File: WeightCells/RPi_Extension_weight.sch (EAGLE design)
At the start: 23 parts, among them U1 AD7730BRUZ, U2 AD7730BRUZ, U3 AD7730BRUZ, U4 AD7730BRUZ, U5 AD7730BRUZ, U6 AD7730BRUZ, U7 AD7730BRUZ, U8 AD7730BRUZ, U9 STM32F103RCT6

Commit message: updated scale board
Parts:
- removed U3, U4, U5, U6, U7, U8: AD7730BRUZ, AD7730BRUZ:AD7730BRUZ
- added C2, C3, C4, C5, C6: (no value), rcl:C-EUC0603
- added SV4: (no value), con-lstb:MA03-2
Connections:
- new net N$2: SV1.1
- new net N$3: SV1.4
- new net N$4: SV1.3
- new net NRST: SV4.6, U9.NRST
- new net SPI1_MISO: U1.DOUT, U2.DOUT, U9.PA6
- new net SPI1_MOSI: U1.DIN, U2.DIN, U9.PA7
- new net SPI1_SCK: U1.SCLK, U2.SCLK, U9.PA5
- new net SS1: U1.*CS, U9.PC6
- new net SS2: U2.*CS, U9.PC7
- new net SS3: U9.PC8
- new net SS4: U9.PC9
- new net SS5: U9.PA8
- new net SS6: U9.PA9
- new net SS7: U9.PA10
- new net SS8: U9.PA11
- new net SS_STACK: SJ5.2, SJ6.2, SJ7.2, SJ8.2
- new net SWDCLK: SV4.3, U9.PA14
- new net SWDIO: SV4.4, U9.PA13
- new net U1_AIN1_+: SV1.16, U1.AIN1(+)
- new net U1_AIN1_-: SV1.15, U1.AIN1(-)
- new net U1_AIN2_+: SV1.14, U1.AIN2(+)D1
- new net U1_AIN2_-: SV1.13, U1.AIN2(-)D0
- new net U1_MCLK_OUT: U1.MCLK_OUT, U2.MCLK_IN
- net +5V: now also U1.REF_IN(+), U2.AVDD
- net DVCC: now also C2.2, C3.1, C4.1, C5.1, C6.1, SV4.1, U1.*RESET, U1.*STANDBY, U1.*SYNC, U2.DVDD, U9.VBAT, U9.VDDA, U9.VDD_1, U9.VDD_2, U9.VDD_3, U9.VDD_4
- net GND: now also C2.1, C3.2, C4.2, C5.2, C6.2, SV4.2, SV4.5, U1.POL, U1.REF_IN(-), U9.VSSA, U9.VSS_1, U9.VSS_2, U9.VSS_3, U9.VSS_4; no longer SV1.10, SV1.12, SV1.14, SV1.16, SV1.2, SV1.4, SV1.6, SV1.8, SV2.10, SV2.12, SV2.14, SV2.16, SV2.2, SV2.4, SV2.6, SV2.8, U3.AGND, U3.DGND, U4.AGND, U4.DGND, U5.AGND, U5.DGND, U6.AGND, U6.DGND, U7.AGND, U7.DGND, U8.AGND, U8.DGND
- net SYNC: no longer SJ5.2, SJ6.2, SJ7.2, SJ8.2
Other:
- moved on the sheet: C1, SV1, SV2, U$1, U1, U2, U9

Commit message: finished top layer of scale board
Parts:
- added U3, U4: AD7730BRUZ, AD7730BRUZ:AD7730BRUZ
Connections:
- removed net SYNC: SJ1.2, SJ2.2, SJ3.2, SJ4.2
- new net U2_MCLK_OUT: U2.MCLK_OUT, U3.MCLK_IN
- new net U3_MCLK_OUT: U3.MCLK_OUT, U4.MCLK_IN
- net +5V: now also U2.REF_IN(+), U3.AVDD, U3.REF_IN(+), U4.AVDD, U4.REF_IN(+)
- net DVCC: now also U2.*RESET, U2.*STANDBY, U2.*SYNC, U3.*RESET, U3.*STANDBY, U3.*SYNC, U3.DVDD, U4.*RESET, U4.*STANDBY, U4.*SYNC, U4.DVDD
- net GND: now also U2.POL, U2.REF_IN(-), U3.AGND, U3.DGND, U3.POL, U3.REF_IN(-), U4.AGND, U4.DGND, U4.POL, U4.REF_IN(-)
- net SPI1_MISO: now also U3.DOUT, U4.DOUT
- net SPI1_MOSI: now also U3.DIN, U4.DIN
- net SPI1_SCK: now also U3.SCLK, U4.SCLK
- net SS1: now also U9.PC9; no longer U9.PC6
- net SS2: now also U9.PC8; no longer U9.PC7
- net SS3: now also U3.*CS, U9.PC7; no longer U9.PC8
- net SS4: now also U4.*CS, U9.PC6; no longer U9.PC9
- net SS_STACK: now also SJ1.2, SJ2.2, SJ3.2, SJ4.2

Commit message: finished top layer of scale board
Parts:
- added U5: AD7730BRUZ, AD7730BRUZ:AD7730BRUZ
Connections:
- new net U4_MCLK_OUT: U4.MCLK_OUT, U5.MCLK_IN
- net +5V: now also U5.AVDD, U5.REF_IN(+)
- net DVCC: now also U5.*RESET, U5.*STANDBY, U5.*SYNC, U5.DVDD
- net GND: now also U5.AGND, U5.DGND, U5.POL, U5.REF_IN(-)
- net SPI1_MISO: now also U5.DOUT
- net SPI1_MOSI: now also U5.DIN
- net SPI1_SCK: now also U5.SCLK
- net SS5: now also U5.*CS
- net U1_AIN1_+: no longer U1.AIN1(+)
- net U1_AIN1_-: no longer U1.AIN1(-)
- net U1_AIN2_+: no longer U1.AIN2(+)D1
- net U1_AIN2_-: no longer U1.AIN2(-)D0

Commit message: updated design
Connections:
- net N$2 renamed U4_AIN2_-
- net N$3 renamed U4_AIN1_+
- net N$4 renamed U4_AIN1_-
- new net N$1: U1.AIN1(-)
- new net N$10: U3.AIN1(+)
- new net N$11: U3.AIN2(+)D1
- new net N$12: U3.AIN2(-)D0
- new net N$13: U4.AIN1(-)
- new net N$14: U4.AIN1(+)
- new net N$15: U4.AIN2(+)D1
- new net N$16: U4.AIN2(-)D0
- new net N$2: U1.AIN1(+)
- new net N$3: U1.AIN2(+)D1
- new net N$4: U1.AIN2(-)D0
- new net N$5: U2.AIN1(-)
- new net N$6: U2.AIN1(+)
- new net N$7: U2.AIN2(+)D1
- new net N$8: U2.AIN2(-)D0
- new net N$9: U3.AIN1(-)
- new net U2_AIN1_+: SV1.12
- new net U2_AIN1_-: SV1.11
- new net U2_AIN2_+: SV1.10
- new net U2_AIN2_-: SV1.9
- new net U3_AIN1_+: SV1.8
- new net U3_AIN1_-: SV1.7
- new net U3_AIN2_+: SV1.6
- new net U3_AIN2_-: SV1.5
- new net U4_AIN2_+: SV1.2
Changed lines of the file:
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@@
 </segment>
 </net>
-<net name="N$2" class="0">
+<net name="U4_AIN2_-" class="0">
 <segment>
 <pinref part="SV1" gate="1" pin="1"/>
 <wire x1="63.5" y1="193.04" x2="58.42" y2="193.04" width="0.1524" layer="91"/>
-<label x="50.8" y="193.04" size="1.778" layer="95"/>
-</segment>
-</net>
-<net name="N$3" class="0">
+<label x="45.72" y="193.04" size="1.778" layer="95"/>
+</segment>
+</net>
+<net name="U4_AIN1_+" class="0">
 <segment>
 <pinref part="SV1" gate="1" pin="4"/>
@@
 </segment>
 </net>
-<net name="N$4" class="0">
+<net name="U4_AIN1_-" class="0">
 <segment>
 <pinref part="SV1" gate="1" pin="3"/>
 <wire x1="63.5" y1="190.5" x2="58.42" y2="190.5" width="0.1524" layer="91"/>
-<label x="50.8" y="190.5" size="1.778" layer="95"/>
+<label x="45.72" y="190.5" size="1.778" layer="95"/>
 </segment>
 </net>
@@
 </segment>
 </net>
+<net name="U4_AIN2_+" class="0">
+<segment>
+<pinref part="SV1" gate="1" pin="2"/>
+<wire x1="78.74" y1="193.04" x2="83.82" y2="193.04" width="0.1524" layer="91"/>
+<label x="83.82" y="193.04" size="1.778" layer="95"/>
+</segment>
+</net>
+<net name="U3_AIN2_+" class="0">
+<segment>
+<pinref part="SV1" gate="1" pin="6"/>
+<wire x1="78.74" y1="187.96" x2="83.82" y2="187.96" width="0.1524" layer="91"/>
+<label x="83.82" y="187.96" size="1.778" layer="95"/>
+</segment>
+</net>
+<net name="U3_AIN1_+" class="0">
+<segment>
+<pinref part="SV1" gate="1" pin="8"/>
+<wire x1="78.74" y1="185.42" x2="83.82" y2="185.42" width="0.1524" layer="91"/>
+<label x="83.82" y="185.42" size="1.778" layer="95"/>
+</segment>
+</net>
+<net name="U2_AIN2_+" class="0">
+<segment>
+<pinref part="SV1" gate="1" pin="10"/>
+<wire x1="78.74" y1="182.88" x2="83.82" y2="182.88" width="0.1524" layer="91"/>
+<label x="83.82" y="182.88" size="1.778" layer="95"/>
+</segment>
+</net>
+<net name="U3_AIN2_-" class="0">
+<segment>
+<pinref part="SV1" gate="1" pin="5"/>
+<wire x1="63.5" y1="187.96" x2="58.42" y2="187.96" width="0.1524" layer="91"/>
+<label x="45.72" y="187.96" size="1.778" layer="95"/>
+</segment>
+</net>
+<net name="U3_AIN1_-" class="0">
+<segment>
+<pinref part="SV1" gate="1" pin="7"/>
+<wire x1="63.5" y1="185.42" x2="58.42" y2="185.42" width="0.1524" layer="91"/>
+<label x="45.72" y="185.42" size="1.778" layer="95"/>
+</segment>
+</net>
+<net name="U2_AIN2_-" class="0">
+<segment>
+<pinref part="SV1" gate="1" pin="9"/>
+<wire x1="63.5" y1="182.88" x2="58.42" y2="182.88" width="0.1524" layer="91"/>
+<label x="45.72" y="182.88" size="1.778" layer="95"/>
+</segment>
+</net>
+<net name="U2_AIN1_-" class="0">
+<segment>
+<pinref part="SV1" gate="1" pin="11"/>
+<wire x1="63.5" y1="180.34" x2="58.42" y2="180.34" width="0.1524" layer="91"/>
+<label x="45.72" y="180.34" size="1.778" layer="95"/>
+</segment>
+</net>
+<net name="U2_AIN1_+" class="0">
+<segment>
+<pinref part="SV1" gate="1" pin="12"/>
+<wire x1="78.74" y1="180.34" x2="83.82" y2="180.34" width="0.1524" layer="91"/>
+<label x="83.82" y="180.34" size="1.778" layer="95"/>
+</segment>
+</net>
+<net name="N$1" class="0">
+<segment>
+<pinref part="U1" gate="A" pin="AIN1(-)"/>
+<wire x1="149.86" y1="182.88" x2="144.78" y2="182.88" width="0.1524" layer="91"/>
+</segment>
+</net>
+<net name="N$2" class="0">
+<segment>
+<pinref part="U1" gate="A" pin="AIN1(+)"/>
+<wire x1="149.86" y1="180.34" x2="144.78" y2="180.34" width="0.1524" layer="91"/>
+</segment>
+</net>
+<net name="N$3" class="0">
+<segment>
+<pinref part="U1" gate="A" pin="AIN2(+)D1"/>
+<wire x1="149.86" y1="177.8" x2="144.78" y2="177.8" width="0.1524" layer="91"/>
+</segment>
+</net>
+<net name="N$4" class="0">
+<segment>
+<pinref part="U1" gate="A" pin="AIN2(-)D0"/>
+<wire x1="149.86" y1="175.26" x2="144.78" y2="175.26" width="0.1524" layer="91"/>
+</segment>
+</net>
+<net name="N$5" class="0">
+<segment>
+<pinref part="U2" gate="A" pin="AIN1(-)"/>
+<wire x1="276.86" y1="182.88" x2="271.78" y2="182.88" width="0.1524" layer="91"/>
+</segment>
+</net>
+<net name="N$6" class="0">
+<segment>
+<pinref part="U2" gate="A" pin="AIN1(+)"/>
+<wire x1="276.86" y1="180.34" x2="271.78" y2="180.34" width="0.1524" layer="91"/>
+</segment>
+</net>
+<net name="N$7" class="0">
+<segment>
+<pinref part="U2" gate="A" pin="AIN2(+)D1"/>
+<wire x1="276.86" y1="177.8" x2="271.78" y2="177.8" width="0.1524" layer="91"/>
+</segment>
+</net>
+<net name="N$8" class="0">
+<segment>
+<pinref part="U2" gate="A" pin="AIN2(-)D0"/>
+<wire x1="276.86" y1="175.26" x2="271.78" y2="175.26" width="0.1524" layer="91"/>
+</segment>
+</net>
+<net name="N$9" class="0">
+<segment>
+<pinref part="U3" gate="A" pin="AIN1(-)"/>
+<wire x1="414.02" y1="182.88" x2="408.94" y2="182.88" width="0.1524" layer="91"/>
+</segment>
+</net>
+<net name="N$10" class="0">
+<segment>
+<pinref part="U3" gate="A" pin="AIN1(+)"/>
+<wire x1="414.02" y1="180.34" x2="408.94" y2="180.34" width="0.1524" layer="91"/>
+</segment>
+</net>
+<net name="N$11" class="0">
+<segment>
+<pinref part="U3" gate="A" pin="AIN2(+)D1"/>
+<wire x1="414.02" y1="177.8" x2="408.94" y2="177.8" width="0.1524" layer="91"/>
+</segment>
+</net>
+<net name="N$12" class="0">
+<segment>
+<pinref part="U3" gate="A" pin="AIN2(-)D0"/>
+<wire x1="414.02" y1="175.26" x2="408.94" y2="175.26" width="0.1524" layer="91"/>
+</segment>
+</net>
+<net name="N$13" class="0">
+<segment>
+<pinref part="U4" gate="A" pin="AIN1(-)"/>
+<wire x1="551.18" y1="185.42" x2="546.1" y2="185.42" width="0.1524" layer="91"/>
+</segment>
+</net>
+<net name="N$14" class="0">
+<segment>
+<pinref part="U4" gate="A" pin="AIN1(+)"/>
+<wire x1="551.18" y1="182.88" x2="546.1" y2="182.88" width="0.1524" layer="91"/>
+</segment>
+</net>
+<net name="N$15" class="0">
+<segment>
+<pinref part="U4" gate="A" pin="AIN2(+)D1"/>
+<wire x1="551.18" y1="180.34" x2="546.1" y2="180.34" width="0.1524" layer="91"/>
+</segment>
+</net>
+<net name="N$16" class="0">
+<segment>
+<pinref part="U4" gate="A" pin="AIN2(-)D0"/>
+<wire x1="551.18" y1="177.8" x2="546.1" y2="177.8" width="0.1524" layer="91"/>
+</segment>
+</net>

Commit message: added second set of transducers
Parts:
- added U6, U7, U8: AD7730BRUZ, AD7730BRUZ:AD7730BRUZ
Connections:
- new net U5_MCLK_OUT: U5.MCLK_OUT, U6.MCLK_IN
- new net U6_MCLK_OUT: U6.MCLK_OUT, U7.MCLK_IN
- new net U7_MCLK_OUT: U7.MCLK_OUT, U8.MCLK_IN
- net +5V: now also U6.AVDD, U6.REF_IN(+), U7.AVDD, U7.REF_IN(+), U8.AVDD, U8.REF_IN(+)
- net DVCC: now also U6.*RESET, U6.*STANDBY, U6.*SYNC, U6.DVDD, U7.*RESET, U7.*STANDBY, U7.*SYNC, U7.DVDD, U8.*RESET, U8.*STANDBY, U8.*SYNC, U8.DVDD
- net GND: now also U6.AGND, U6.DGND, U6.POL, U6.REF_IN(-), U7.AGND, U7.DGND, U7.POL, U7.REF_IN(-), U8.AGND, U8.DGND, U8.POL, U8.REF_IN(-)
- net SPI1_MISO: now also U6.DOUT, U7.DOUT, U8.DOUT
- net SPI1_MOSI: now also U6.DIN, U7.DIN, U8.DIN
- net SPI1_SCK: now also U6.SCLK, U7.SCLK, U8.SCLK
- net SS5: now also U9.PC3; no longer U9.PA8
- net SS6: now also U6.*CS, U9.PC2; no longer U9.PA9
- net SS7: now also U7.*CS, U9.PC1; no longer U9.PA10
- net SS8: now also U8.*CS, U9.PC0; no longer U9.PA11

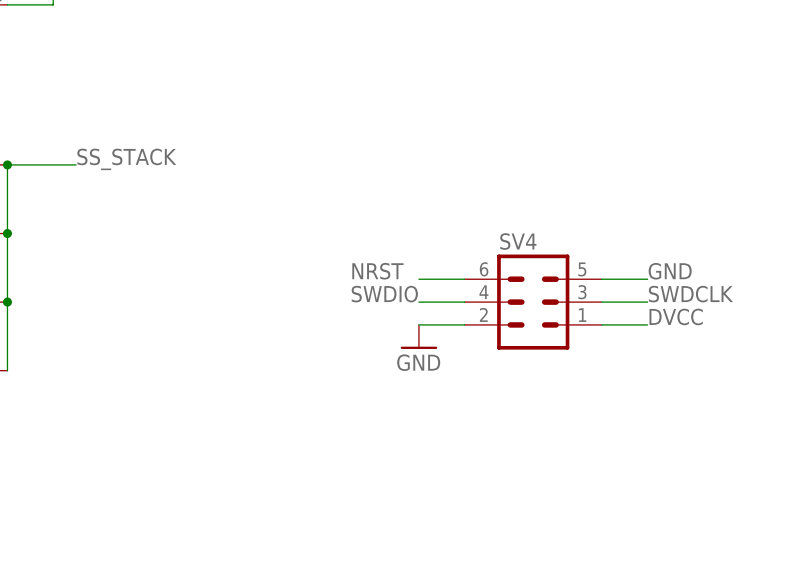
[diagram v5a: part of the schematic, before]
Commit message: shifted top ics and rerouted some signals for compliance
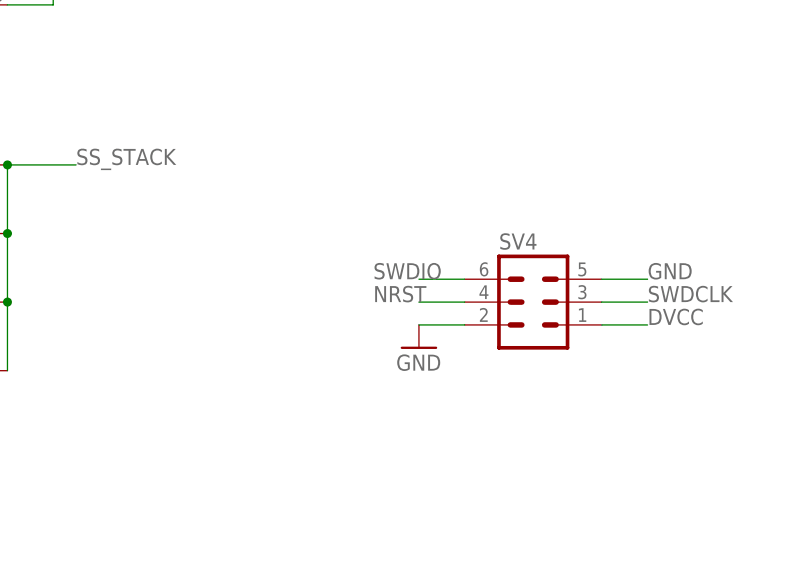
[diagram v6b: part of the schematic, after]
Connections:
- net NRST: now also SV4.4; no longer SV4.6
- net SWDIO: now also SV4.6; no longer SV4.4
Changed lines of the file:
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@@
 <net name="SWDIO" class="0">
-<segment>
-<wire x1="58.42" y1="15.24" x2="53.34" y2="15.24" width="0.1524" layer="91"/>
-<label x="45.72" y="15.24" size="1.778" layer="95"/>
-<pinref part="SV4" gate="1" pin="4"/>
-</segment>
 <segment>
 <pinref part="U9" gate="A" pin="PA13"/>
 <wire x1="152.4" y1="-35.56" x2="144.78" y2="-35.56" width="0.1524" layer="91"/>
 <label x="134.62" y="-35.56" size="1.778" layer="95"/>
+</segment>
+<segment>
+<pinref part="SV4" gate="1" pin="6"/>
+<wire x1="58.42" y1="17.78" x2="53.34" y2="17.78" width="0.1524" layer="91"/>
+<label x="48.26" y="17.78" size="1.778" layer="95"/>
 </segment>
 </net>
@@
 <net name="NRST" class="0">
 <segment>
-<wire x1="58.42" y1="17.78" x2="53.34" y2="17.78" width="0.1524" layer="91"/>
-<label x="45.72" y="17.78" size="1.778" layer="95"/>
-<pinref part="SV4" gate="1" pin="6"/>
-</segment>
-<segment>
 <pinref part="U9" gate="A" pin="NRST"/>
 <wire x1="213.36" y1="20.32" x2="220.98" y2="20.32" width="0.1524" layer="91"/>
 <label x="220.98" y="20.32" size="1.778" layer="95"/>
 </segment>
+<segment>
+<pinref part="SV4" gate="1" pin="4"/>
+<wire x1="58.42" y1="15.24" x2="53.34" y2="15.24" width="0.1524" layer="91"/>
+<label x="48.26" y="15.24" size="1.778" layer="95"/>
+</segment>
 </net>

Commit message: added traces to load cell connectors
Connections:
- removed net N$1: U1.AIN1(-)
- removed net N$10: U3.AIN1(+)
- removed net N$11: U3.AIN2(+)D1
- removed net N$12: U3.AIN2(-)D0
- removed net N$13: U4.AIN1(-)
- removed net N$14: U4.AIN1(+)
- removed net N$15: U4.AIN2(+)D1
- removed net N$16: U4.AIN2(-)D0
- removed net N$2: U1.AIN1(+)
- removed net N$3: U1.AIN2(+)D1
- removed net N$4: U1.AIN2(-)D0
- removed net N$5: U2.AIN1(-)
- removed net N$6: U2.AIN1(+)
- removed net N$7: U2.AIN2(+)D1
- removed net N$8: U2.AIN2(-)D0
- removed net N$9: U3.AIN1(-)
- new net U5_AIN1_+: SV2.2, U5.AIN1(+)
- new net U5_AIN1_-: SV2.1, U5.AIN1(-)
- new net U5_AIN2_+: SV2.4, U5.AIN2(+)D1
- new net U5_AIN2_-: SV2.3, U5.AIN2(-)D0
- new net U6_AIN1_+: SV2.6, U6.AIN1(+)
- new net U6_AIN1_-: SV2.5, U6.AIN1(-)
- new net U6_AIN2_+: SV2.8, U6.AIN2(+)D1
- new net U6_AIN2_-: SV2.7, U6.AIN2(-)D0
- new net U7_AIN1_+: SV2.10, U7.AIN1(+)
- new net U7_AIN1_-: SV2.9, U7.AIN1(-)
- new net U7_AIN2_+: SV2.12, U7.AIN2(+)D1
- new net U7_AIN2_-: SV2.11, U7.AIN2(-)D0
- new net U8_AIN1_+: SV2.14, U8.AIN1(+)
- new net U8_AIN1_-: SV2.13, U8.AIN1(-)
- new net U8_AIN2_+: SV2.16, U8.AIN2(+)D1
- new net U8_AIN2_-: SV2.15, U8.AIN2(-)D0
- net U1_AIN1_+: now also U1.AIN1(+)
- net U1_AIN1_-: now also U1.AIN1(-)
- net U1_AIN2_+: now also U1.AIN2(+)D1
- net U1_AIN2_-: now also U1.AIN2(-)D0
- net U2_AIN1_+: now also U2.AIN1(+)
- net U2_AIN1_-: now also U2.AIN1(-)
- net U2_AIN2_+: now also U2.AIN2(+)D1
- net U2_AIN2_-: now also U2.AIN2(-)D0
- net U3_AIN1_+: now also U3.AIN1(+)
- net U3_AIN1_-: now also U3.AIN1(-)
- net U3_AIN2_+: now also U3.AIN2(+)D1
- net U3_AIN2_-: now also U3.AIN2(-)D0
- net U4_AIN1_+: now also U4.AIN1(+)
- net U4_AIN1_-: now also U4.AIN1(-)
- net U4_AIN2_+: now also U4.AIN2(+)D1
- net U4_AIN2_-: now also U4.AIN2(-)D0
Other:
- moved on the sheet: SV3
